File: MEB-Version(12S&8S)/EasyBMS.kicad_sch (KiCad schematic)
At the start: 174 parts, among them IC1 XL7046, IC2 LTC6811IG-1#PBF, IC3 ISO1042DWV, IC4 AMS1117-3.3, J1 TYPE-C-31-M-12, Q14 CJ2301, Q15 CJ2301, Q16 CJ2301, Q18 CJ2301, Q20 CJ2301, Q22 CJ2301, Q24 CJ2301, Q26 CJ2301, Q28 CJ2301, Q30 CJ2301, Q32 CJ2301, Q34 CJ2301, U1 ESP32-C6-MINI-1-N4, Y1 FC-135_32.7680KA-A5

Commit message: new grounding with one common ground
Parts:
- removed C12: 47µF, EasyBMS:C1206_334, symbol EasyBMS-eagle-import:C-EUC1206
- removed C2: 100µF/16V, EasyBMS:153CLV-0605_334, symbol EasyBMS-eagle-import:CPOL-EU153CLV-0605
- removed C3: 100nF, EasyBMS:C0402_334, symbol EasyBMS-eagle-import:C-EUC0402
- removed C7: 1uF, EasyBMS:C0402_334, symbol EasyBMS-eagle-import:C-EUC0402
- removed CSLTC0, MISO0: SJ, EasyBMS:SJ_252, symbol EasyBMS-eagle-import:SJ
- removed R59: 600R@100MHz, EasyBMS:R1206_334, symbol EasyBMS-eagle-import:R-EU_R1206
- added C18, C22, C30: 22uF, EasyBMS:C0603_334, symbol EasyBMS-eagle-import:C-EUC0603
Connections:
- net GND2 is gone; now on net GND: C1.2, C19.2, C20.1, C23.2, C4.2, D1.A, D7.C, IC2.30 (V-_1), IC2.31 (V-_2), IC2.40 (ISOMD), R17.1, R4.1, R57.1, R58.1, R8.1
- net +5V: now also C22.1
- net +5V/1: now also C18.1
- net C1-: now also D1.C, D7.A
- net GND: now also C18.2, C22.2; no longer D1.C, D7.A
- net at C11.2, IC3.5 (GND2), JP7.4: now also C30.2
- net at C11.1, IC3.8 (VCC2), JP7.1: now also C30.1
- no-connect marks 6 -> 11
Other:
- moved on the sheet: D1, D7, JP1, R18

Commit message: add ESD protection to CAN, more clearance on high voltage diff
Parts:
- removed D11, D13, D9: LESD5D5.0CT1G, EasyBMS:SOD523_210, symbol EasyBMS-eagle-import:DIODE-SOD523
- removed IC3: ISO1042DWV, EasyBMS:SOIC127P1150X280-8N, symbol EasyBMS-eagle-import:ISO1042DWV
- removed JP7: 2828XX-4282834-4, EasyBMS:TERMBLK_254-4N_16378166, symbol EasyBMS-eagle-import:2828XX-4282834-4
- added D11, D17, D37, D9: LESD5D5.0CT1G_C5199850, EasyEDA2KiCAD:SOD-523_L1.2-W0.8-LS1.6-BI, symbol EasyEDA2KiCAD:LESD5D5.0CT1G_C5199850
- added D35: PESD1CAN,215, EasyEDA2KiCAD:SOT-23_L2.9-W1.3-P1.90-LS2.4-BR, symbol EasyEDA2KiCAD:PESD1CAN,215
- added F1, F2: 60V 100mA/JK-NSMD010, Resistor_SMD:R_1206_3216Metric, symbol Device:Fuse
- added J2: Screw_Terminal_01x04, TerminalBlock_TE-Connectivity:TerminalBlock_TE_282834-4_1x04_P2.54mm_Horizontal, symbol Connector:Screw_Terminal_01x04
- added U5: CA-IS3050CG, Package_SO:SOIC-8_7.5x5.85mm_P1.27mm, symbol Interface_CAN_LIN:ISO1050DUB
- IC1: footprint EasyBMS:SOIC127P600X170-9N -> EasyEDA2KiCAD:ESOP-8_L4.9-W3.9-P1.27-LS6.0-TL-EP
- LED2: footprint EasyBMS:XL-1615RGBC-WS2812B -> EasyEDA2KiCAD:LED-SMD_4P-L1.6-W1.5_XL-1615RGBC-WS2812B-1
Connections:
- net +3V3: now also U5.1 (VCC1)
- net +5V/1: now also LED2.3 (VDD); no longer LED2.VDD
- net D+: now also D11.2
- net D-: now also D9.2
- net GND: now also LED2.1 (GND), D11.1, D17.1, D9.1, U5.4 (GND1); no longer LED2.VSS (GND)
- net at U1.28 (IO22): now also U5.2 (RXD)
- net at U1.29 (IO23): now also U5.3 (TXD)
- net at D2.A, J1.A4_B9 (VBUS), J1.B4_A9 (VBUS): now also D17.2
- net at C11.2, C30.2: now also D35.3, D37.1, J2.4 (Pin_4), U5.5 (GND2)
- net at R12.1: now also F2.2, J2.3 (Pin_3)
- net at TERM0.1: now also F1.2, J2.2 (Pin_2)
- net at C11.1, C30.1: now also D37.2, J2.1 (Pin_1), U5.8 (VCC2)
- net at D15.2 (A), R21.2: now also LED2.2 (DI); no longer LED2.DIN (DI)
- new net: D35.2, F2.1, U5.6 (CANL)
- new net: D35.1, F1.1, U5.7 (CANH)
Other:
- moved on the sheet: C10, C11, C30, R12, TERM0

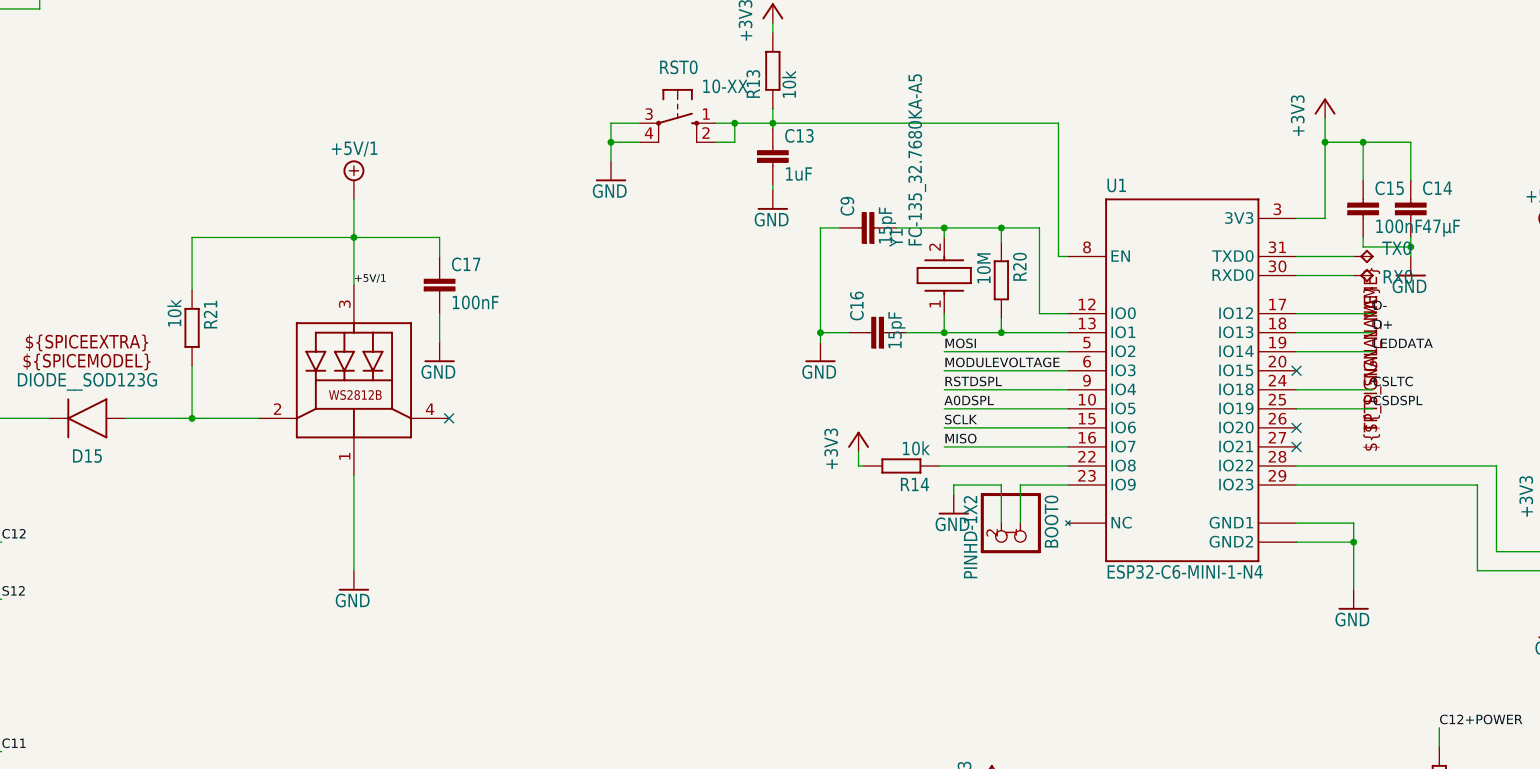
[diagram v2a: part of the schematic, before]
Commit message: changed RGB LED and new simple red LED
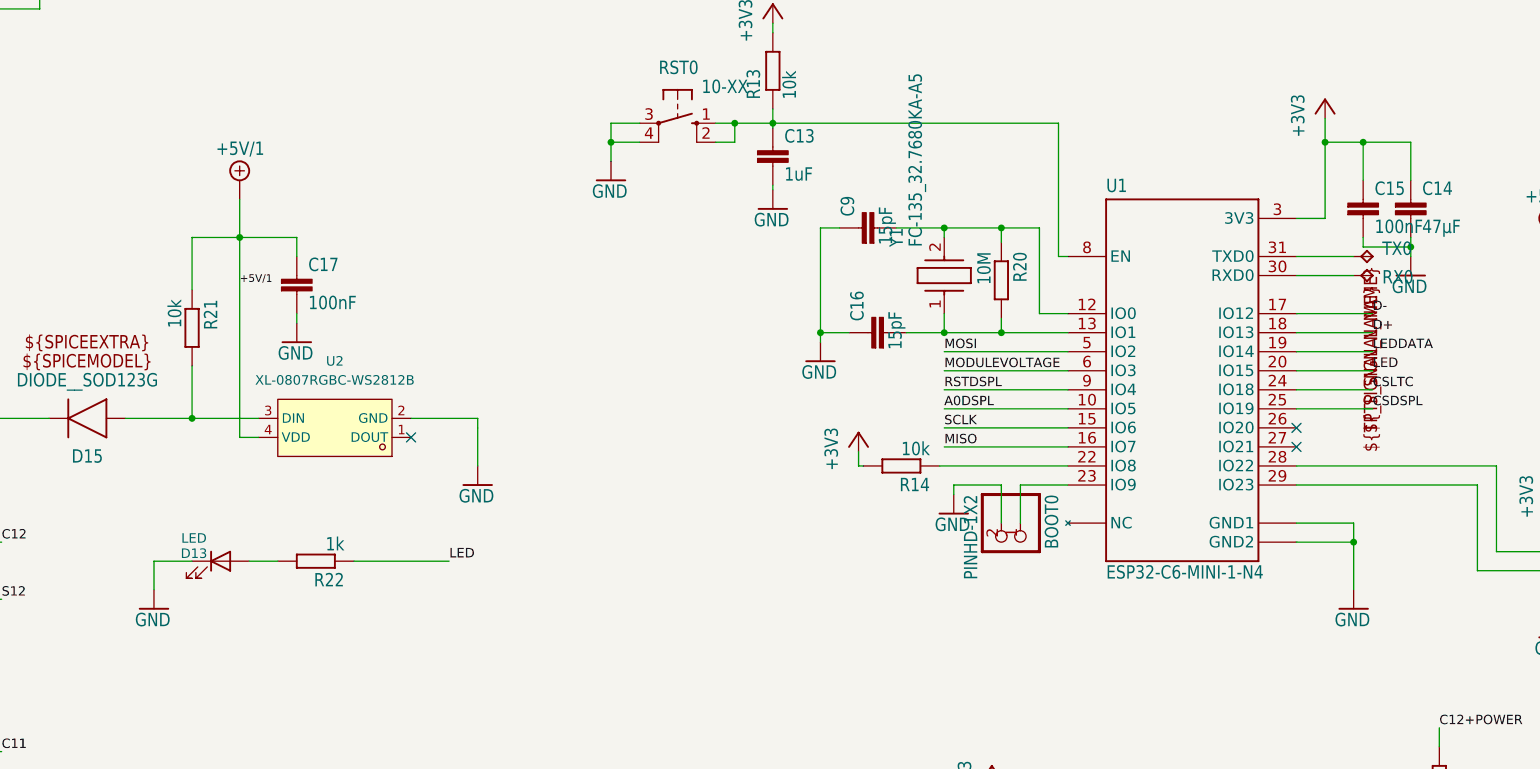
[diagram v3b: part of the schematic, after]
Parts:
- removed LED2: XL-1615RGBC-WS2812B, EasyEDA2KiCAD:LED-SMD_4P-L1.6-W1.5_XL-1615RGBC-WS2812B-1, symbol EasyBMS-eagle-import:XL-1615RGBC-WS2812B
- added D13: LED, LED_SMD:LED_0603_1608Metric, symbol Device:LED
- added R22: 1k, EasyBMS:R0402_334, symbol EasyBMS-eagle-import:R-EU_R0402
- added U2: XL-0807RGBC-WS2812B, EasyEDA2KiCAD:LED-SMD_4P-L2.0-W1.8_XL-0807RGBC-WS2812B, symbol EasyEDA2KiCAD:XL-0807RGBC-WS2812B
- BOOT0, D10, D12, D14, D16, D18, D20, D22, D24, D4, D5, D6, D8, H1, H2, H3, JP1, JP10, JP11, JP12, JP13, JP2, JP3, JP4, JP5, JP6, JP8, JP9, RST0, RX0, TERM0, TX0: now left out of the parts list
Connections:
- net +5V/1: now also U2.4 (VDD)
- net GND: now also D13.1 (K), U2.2 (GND)
- net LED: now reaches U1.20 (IO15)
- net LED: now also R22.1
- net at D15.2 (A), R21.2: now also U2.3 (DIN)
- new net: D13.2 (A), R22.2
- no-connect marks 11 -> 10
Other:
- moved on the sheet: C17

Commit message: replace old imported symbols and footprints with kicad ones
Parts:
- removed H1, H2, H3: MOUNT-HOLE3.2, EasyBMS:3,2_237, symbol EasyBMS-eagle-import:MOUNT-HOLE3.2
- removed IC1: XL7046, EasyEDA2KiCAD:ESOP-8_L4.9-W3.9-P1.27-LS6.0-TL-EP, symbol EasyBMS-eagle-import:XL7046
- removed IC2: LTC6811IG-1#PBF, EasyBMS:SOP50P780X200-48N, symbol EasyBMS-eagle-import:LTC6811IG-1#PBF
- removed L1: 100µH, EasyBMS:CY75-100UH, symbol EasyBMS-eagle-import:CY75-100UH
- removed U1: ESP32-C6-MINI-1-N4, EasyBMS:XCVR_ESP32-C6-MINI-1-N4, symbol EasyBMS-eagle-import:ESP32-C6-MINI-1-N4
- added L2: 100µH, EasyEDA2KiCAD:IND-SMD_L7.8-W7.0-A, symbol Device:L_Ferrite
- added U1: ESP32-C6-MINI-1, RF_Module:ESP32-C6-MINI-1, symbol RF_Module:ESP32-C6-MINI-1
- added U3: LTC6811-1, Package_SO:SSOP-48_5.3x12.8mm_P0.5mm, symbol Battery_Management:LTC6804-1
- added U4: XL7046, EasyEDA2KiCAD:ESOP-8_L4.9-W3.9-P1.27-LS6.0-TL-EP, symbol EasyEDA2KiCAD:XL7046
- BOOT0: footprint EasyBMS:1X02 -> Connector_PinHeader_2.54mm:PinHeader_1x02_P2.54mm_Vertical; symbol EasyBMS-eagle-import:PINHD-1X2 -> Jumper:Jumper_2_Open; now in the parts list
- C1, C10, C11, C13, C15, C16, C17, C19, C23, C25, C28, C29, C31, C33, C35, C37, C39, C4, C41, C43, C45, C47, C5, C6, C9: footprint EasyBMS:C0402_334 -> Capacitor_SMD:C_0402_1005Metric; symbol EasyBMS-eagle-import:C-EUC0402 -> Device:C
- C14, C20, C21: footprint EasyBMS:C0805_334 -> Capacitor_SMD:C_0805_2012Metric; symbol EasyBMS-eagle-import:C-EUC0805 -> Device:C
- C18, C22, C27, C30, C8: footprint EasyBMS:C0603_334 -> Capacitor_SMD:C_0603_1608Metric; symbol EasyBMS-eagle-import:C-EUC0603 -> Device:C
- C24: footprint EasyBMS:153CLV-0605_334 -> Capacitor_SMD:CP_Elec_6.3x5.4; symbol EasyBMS-eagle-import:CPOL-EU153CLV-0605 -> Device:C_Polarized
- C26: footprint EasyBMS:153CLV-0605_334 -> Capacitor_SMD:CP_Elec_6.3x7.7; symbol EasyBMS-eagle-import:CPOL-EU153CLV-0605 -> Device:C_Polarized
- D1, D2, D3, D7: footprint EasyBMS:DO214AC_210 -> Diode_SMD:D_SMA; symbol EasyBMS-eagle-import:DIODE-DO214AC -> Diode:SS210
- D10, D12, D14, D16, D18, D20, D22, D24, D4, D5, D6, D8: footprint EasyBMS:MELF-MLL34 -> Diode_SMD:D_MiniMELF; symbol EasyBMS-eagle-import:D-FILL-MLL-34 -> Diode:ZMMxx; now in the parts list
- D11, D17, D37, D9: footprint EasyEDA2KiCAD:SOD-523_L1.2-W0.8-LS1.6-BI -> Diode_SMD:D_SOD-523
- D15: footprint EasyBMS:SOD3715X135_16378169 -> Diode_SMD:D_SOD-123; symbol EasyBMS-eagle-import:DIODE__SOD123G -> Diode:1N4148W
- D35: footprint EasyEDA2KiCAD:SOT-23_L2.9-W1.3-P1.90-LS2.4-BR -> Package_TO_SOT_SMD:SOT-23
- IC4: footprint EasyBMS:SOT223_111 -> Package_TO_SOT_SMD:SOT-223-3_TabPin2; symbol EasyBMS-eagle-import:REG1117 -> Regulator_Linear:AMS1117-3.3
- J1: footprint EasyBMS:HRO_TYPE-C-31-M-12 -> Connector_USB:USB_C_Receptacle_HRO_TYPE-C-31-M-12; symbol EasyBMS-eagle-import:TYPE-C-31-M-12 -> Connector:USB_C_Receptacle_USB2.0_14P
- JP1: footprint EasyBMS:1X08_16378166 -> Connector_PinHeader_2.54mm:PinHeader_1x08_P2.54mm_Vertical; symbol EasyBMS-eagle-import:PINHD-1X8 -> Connector:Conn_01x08_Pin; now in the parts list
- JP10, JP11, JP12, JP13, JP2, JP3, JP4, JP5, JP6, JP8, JP9: footprint EasyBMS:1X02 -> Connector_PinHeader_2.54mm:PinHeader_1x02_P2.54mm_Vertical; symbol EasyBMS-eagle-import:pinhead_own_PINHD-1X2 -> Connector:Conn_01x02_Pin; now in the parts list
- Q14, Q15, Q16, Q18, Q20, Q22, Q24, Q26, Q28, Q30, Q32, Q34: footprint EasyBMS:PG-SOT-23 -> Package_TO_SOT_SMD:SOT-23; symbol EasyBMS-eagle-import:BSS308PEH6327XTSA1 -> Transistor_FET:BSS83P
- R1, R17, R3, R7: footprint EasyBMS:R0603_334 -> Resistor_SMD:R_0603_1608Metric; symbol EasyBMS-eagle-import:R-EU_R0603 -> Device:R
- R10, R102, R103, R106, R107, R11, R114, R115, R12, R122, R123, R13, R130, R131, R138, R139, R14, R146, R147, R154, R155, R162, R163, R170, R171, R178, R179, R2, R20, R21, R22, R5, R55, R57, R58, R6, R60, R9, R97, R98: footprint EasyBMS:R0402_334 -> Resistor_SMD:R_0402_1005Metric; symbol EasyBMS-eagle-import:R-EU_R0402 -> Device:R
- R100, R101, R104, R105, R112, R113, R120, R121, R128, R129, R136, R137, R144, R145, R152, R153, R160, R161, R168, R169, R176, R177, R19, R82, R96: footprint EasyBMS:R1206_334 -> Resistor_SMD:R_1206_3216Metric; symbol EasyBMS-eagle-import:R-EU_R1206 -> Device:R
- R15, R16: footprint EasyBMS:R0603_334 -> Resistor_SMD:R_0603_1608Metric; symbol EasyBMS-eagle-import:R-EU_R0402 -> Device:R
- R18: footprint EasyBMS:R1206_334 -> Resistor_SMD:R_1206_3216Metric; symbol EasyBMS-eagle-import:R-EU_R1206 -> Device:FerriteBead
- R4, R8: footprint EasyBMS:R0603_334 -> Resistor_SMD:R_0603_1608Metric; symbol EasyBMS-eagle-import:R-EU_R0603 -> Device:Thermistor_NTC
- RST0: footprint EasyBMS:B3F-10XX_377 -> Button_Switch_THT:SW_PUSH_6mm; symbol EasyBMS-eagle-import:10-XX -> Switch:SW_Push; now in the parts list
- RX0, TX0: footprint EasyBMS:B2,54_385 -> TestPoint:TestPoint_Pad_D2.0mm; symbol EasyBMS-eagle-import:TPB2,54 -> Connector:TestPoint; now in the parts list
- TERM0: footprint EasyBMS:SJ_252 -> Jumper:SolderJumper-2_P1.3mm_Open_RoundedPad1.0x1.5mm; symbol EasyBMS-eagle-import:SJ -> Jumper:SolderJumper_2_Open
- Y1: footprint EasyBMS:FC135327680KAA5 -> EasyEDA2KiCAD:FC-135R_L3.2-W1.5; symbol EasyBMS-eagle-import:FC-135_32.7680KA-A5 -> Device:Crystal
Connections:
- net +3V3: now also U1.3 (3V3)
- net +5V: now also U3.36 (SWTEN), U3.37 (VREG)
- net +5V/1: now also C24.1, D2.1 (K), U4.1 (CSN); no longer C24.+, D2.C
- net A0DSPL: now also U1.10 (IO5)
- net C0: now also U3.26 (C0)
- net C1: now also U3.24 (C1)
- net C1-: now also D1.1 (K), D7.2 (A); no longer D1.C, D7.A
- net C10: now also U3.6 (C10)
- net C11: now also U3.4 (C11)
- net C12: now also U3.2 (C12)
- net C2: now also U3.22 (C2)
- net C3: now also U3.20 (C3)
- net C4: now also U3.18 (C4)
- net C5: now also U3.16 (C5)
- net C6: now also U3.14 (C6)
- net C7: now also U3.12 (C7)
- net C8: now also U3.10 (C8)
- net C9: now also U3.8 (C9)
- net CSDSPL: now also U1.25 (IO19)
- net CSLTC: now also U1.24 (IO18), U3.41 (CSB(IMA))
- net D+: now also U1.18 (IO13)
- net D-: now also U1.17 (IO12)
- net GND: now also BOOT0.1 (A), C24.2, C26.2, D1.2 (A), D3.2 (A), D7.1 (K), J1.A1 (GND), J1.A12 (GND), J1.B1 (GND), J1.B12 (GND), RST0.1, U1.1 (GND), U1.11 (GND), U1.14 (GND), U1.2 (GND), U1.36 (GND), U1.37 (GND), U1.38 (GND), U1.39 (GND), U1.40 (GND), U1.41 (GND), U1.42 (GND), U1.43 (GND), U1.44 (GND), U1.45 (GND), U1.46 (GND), U1.47 (GND), U1.48 (GND), U1.49 (GND), U1.50 (GND), U1.51 (GND), U1.52 (GND), U1.53 (GND), U3.30 (V-), U3.31 (V-), U3.40 (ISOMD), U4.6 (EN), U4.7 (GND); no longer BOOT0.2, C24.-, C26.-, D1.A, D3.A, D7.C, J1.A1_B12 (GND), J1.B1_A12 (GND), RST0.3 (P), RST0.4 (P1)
- net GPIO5: now also U3.33 (GPIO5)
- net IBIAS: now also U3.45 (IBIAS), U3.46 (ICMP)
- net IMB: now also U3.47 (IMB)
- net IPB: now also U3.48 (IPB)
- net LED: now also U1.20 (IO15)
- net LEDDATA: now also U1.19 (IO14)
- net MISO: now also U1.16 (IO7), U3.44 (SDO(NC))
- net MODULEVOLTAGE: now also U1.6 (IO3)
- net MOSI: now also U1.5 (IO2), U3.43 (SDI(NC))
- net RSTDSPL: now also U1.9 (IO4)
- net S1: now also U3.25 (S1)
- net S10: now also U3.7 (S10)
- net S11: now also U3.5 (S11)
- net S12: now also U3.3 (S12)
- net S2: now also U3.23 (S2)
- net S3: now also U3.21 (S3)
- net S4: now also U3.19 (S4)
- net S5: now also U3.17 (S5)
- net S6: now also U3.15 (S6)
- net S7: now also U3.13 (S7)
- net S8: now also U3.11 (S8)
- net S9: now also U3.9 (S9)
- net SCLK: now also U1.15 (IO6), U3.42 (SCK(IPA))
- net V+: no longer C20.2, R9.1
- net VREF1: now also U3.35 (VREF1)
- net VREF2: now also U3.34 (VREF2)
- net VTEMP1: now also U3.27 (GPIO1)
- net VTEMP2: now also U3.28 (GPIO2)
- net VTEMPNORTH: now also U3.32 (GPIO4)
- net VTEMPSOUTH: now also U3.29 (GPIO3)
- net at R5.1: now also L2.2, U4.2 (CSP)
- net at C6.2, R55.2, R6.1: now also U4.8 (FB)
- net at C9.2, R20.1, Y1.2: now also U1.12 (IO0)
- net at C16.2, R20.2, Y1.1: now also U1.13 (IO1)
- net at R14.1: now also U1.22 (IO8)
- net at U5.2 (RXD): now also U1.28 (IO22)
- net at U5.3 (TXD): now also U1.29 (IO23)
- net at C13.1, R13.1, RST0.2: now also U1.8 (EN); no longer RST0.1 (S)
- net at C21.1, C27.1, R19.1: now also C26.1, U4.4 (VIN); no longer C26.+
- net at C27.2: now also U4.3 (VC)
- new net: BOOT0.2 (B), U1.23 (IO9)
- new net: D17.2, D2.2 (A), J1.A4 (VBUS), J1.A9 (VBUS), J1.B4 (VBUS), J1.B9 (VBUS)
- new net: D3.1 (K), L2.1, U4.5 (SW), U4.9 (EP)
- new net: C20.2, R9.1, U3.1 (V+)
- new net: RX0.1, U1.30 (RXD0)
- new net: TX0.1, U1.31 (TXD0)
- no-connect marks 10 -> 8
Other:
- moved on the sheet: D11, D17, D9, JP10, JP11, JP12, JP13, JP2, JP3, JP4, JP5, JP6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
